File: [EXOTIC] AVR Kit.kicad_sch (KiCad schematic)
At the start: 22 parts, among them J1 AVR-ISP-10, J3 USB_B, J4 Port A, J5 Port B, J6 Port C + D7, J7 Port D, SW1 SW_Push, U1 ATmega32A-P, U6 CH340C, Y1 16 MHz

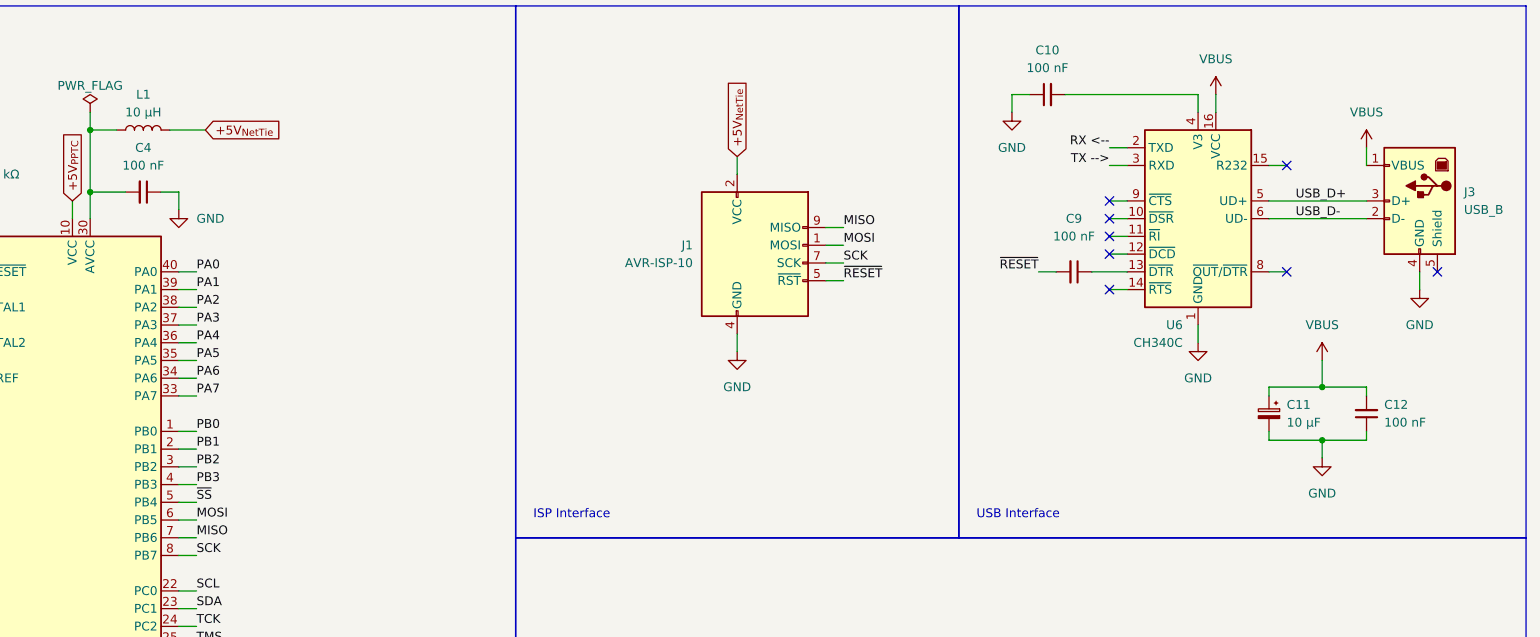
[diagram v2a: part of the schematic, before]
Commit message: Removed the two LED indicators
Removed the two LED indicators for each power source and replaced them with a single LED for the final 5V rail
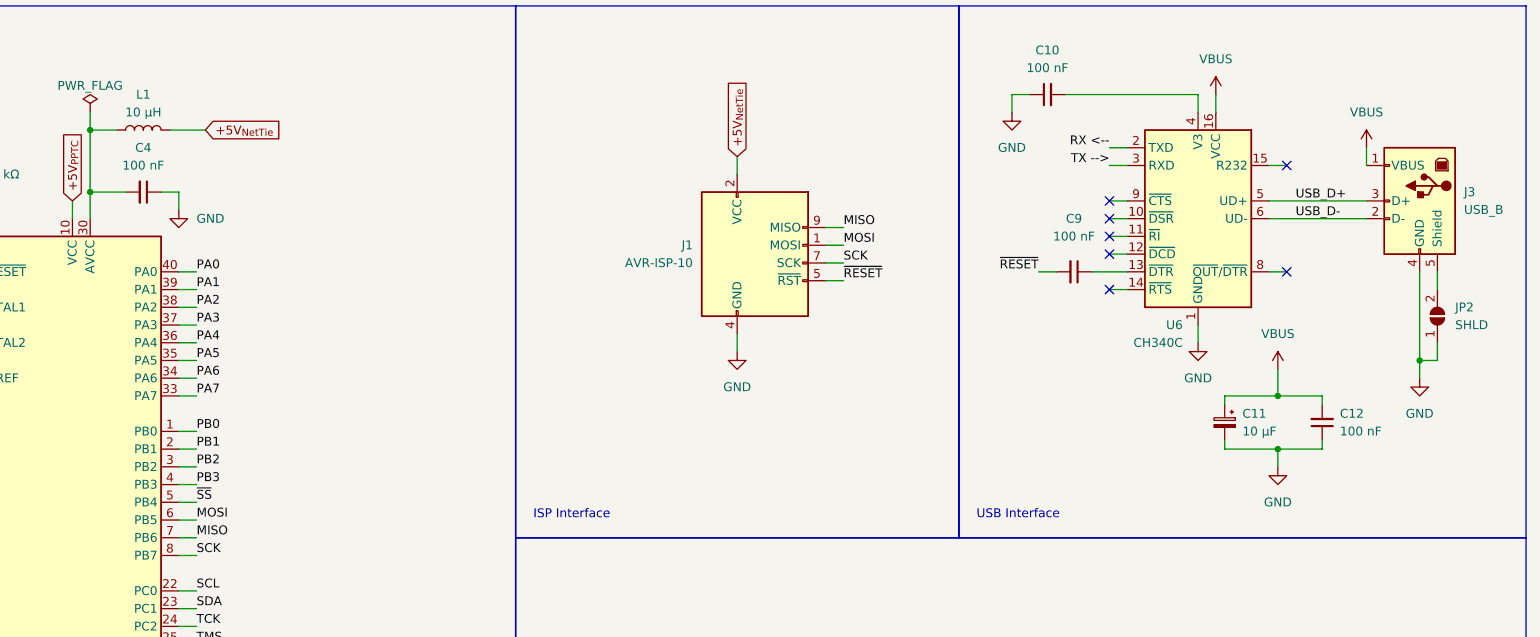
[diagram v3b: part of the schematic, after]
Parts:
- added JP2: SHLD, Jumper:SolderJumper-2_P1.3mm_Open_RoundedPad1.0x1.5mm, symbol Jumper:SolderJumper_2_Open
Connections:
- net +5V_{NetTie}: now also L1.1; no longer L1.2
- net GND: now also JP2.1 (A)
- net at C4.2, U1.30 (AVCC): now also L1.2; no longer L1.1
- net at J3.5 (Shield): now also JP2.2 (B)
- no-connect marks 8 -> 7
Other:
- company: Exotic Racing Team -> Team Exotic
- moved on the sheet: C11, C12, L1
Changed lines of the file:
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@@
 	(title_block
 		(title "ATMEGA32A AVR Kit")
-		(date "2023-10-28")
-		(rev "C1.2")
-		(company "Exotic Racing Team")
+		(date "2024-06-14")
+		(rev "C2.7")
+		(company "Team Exotic")
 		(comment 1 "Author: Morad Tamer")
 	)
@@
 	)
 	(junction
-		(at 255.27 67.31)
+		(at 248.92 68.58)
+		(diameter 0)
+		(color 0 0 0 0)
+	)
+	(junction
+		(at 269.24 63.5)
 		(diameter 0)
 		(color 0 0 0 0)
@@
 	)
 	(junction
-		(at 255.27 74.93)
+		(at 248.92 76.2)
 		(diameter 0)
 		(color 0 0 0 0)
@@
 	)
 	(no_connect
-		(at 271.78 50.8)
-	)
-	(no_connect
 		(at 224.79 45.72)
 	)
@@
 	(wire
 		(pts
-			(xy 247.65 67.31) (xy 247.65 68.58)
+			(xy 241.3 68.58) (xy 241.3 69.85)
 		)
 		(stroke
@@
 	(wire
 		(pts
-			(xy 261.62 73.66) (xy 261.62 74.93)
+			(xy 255.27 74.93) (xy 255.27 76.2)
 		)
 		(stroke
@@
 	(wire
 		(pts
-			(xy 247.65 74.93) (xy 255.27 74.93)
+			(xy 241.3 76.2) (xy 248.92 76.2)
 		)
 		(stroke
@@
 	(wire
 		(pts
+			(xy 271.78 50.8) (xy 271.78 53.34)
+		)
+		(stroke
+			(width 0)
+			(type default)
+		)
+	)
+	(wire
+		(pts
 			(xy 91.44 109.22) (xy 93.98 109.22)
 		)
@@
 	(wire
 		(pts
-			(xy 255.27 63.5) (xy 255.27 67.31)
+			(xy 248.92 64.77) (xy 248.92 68.58)
 		)
 		(stroke
@@
 	(wire
 		(pts
-			(xy 255.27 74.93) (xy 255.27 77.47)
+			(xy 248.92 76.2) (xy 248.92 78.74)
 		)
 		(stroke
@@
 	(wire
 		(pts
-			(xy 255.27 74.93) (xy 261.62 74.93)
+			(xy 248.92 76.2) (xy 255.27 76.2)
 		)
 		(stroke
@@
 	(wire
 		(pts
-			(xy 269.24 50.8) (xy 269.24 53.34)
+			(xy 269.24 50.8) (xy 269.24 63.5)
 		)
 		(stroke
@@
 	(wire
 		(pts
-			(xy 255.27 67.31) (xy 261.62 67.31)
+			(xy 248.92 68.58) (xy 255.27 68.58)
 		)
 		(stroke
@@
 	(wire
 		(pts
+			(xy 271.78 60.96) (xy 271.78 63.5)
+		)
+		(stroke
+			(width 0)
+			(type default)
+		)
+	)
+	(wire
+		(pts
 			(xy 189.23 114.3) (xy 194.31 114.3)
 		)
@@
 	(wire
 		(pts
-			(xy 261.62 67.31) (xy 261.62 68.58)
+			(xy 255.27 68.58) (xy 255.27 69.85)
 		)
 		(stroke
@@
 	(wire
 		(pts
+			(xy 269.24 63.5) (xy 271.78 63.5)
+		)
+		(stroke
+			(width 0)
+			(type default)
+		)
+	)
+	(wire
+		(pts
 			(xy 91.44 76.2) (xy 93.98 76.2)
 		)
@@
 	(wire
 		(pts
+			(xy 269.24 63.5) (xy 269.24 66.04)
+		)
+		(stroke
+			(width 0)
+			(type default)
+		)
+	)
+	(wire
+		(pts
 			(xy 50.8 66.04) (xy 50.8 68.58)
 		)
@@
 	(wire
 		(pts
-			(xy 247.65 67.31) (xy 255.27 67.31)
+			(xy 241.3 68.58) (xy 248.92 68.58)
 		)
 		(stroke
@@
 	(wire
 		(pts
-			(xy 247.65 73.66) (xy 247.65 74.93)
+			(xy 241.3 74.93) (xy 241.3 76.2)
 		)
 		(stroke
@@
 	(symbol
 		(lib_id "power:GND")
-		(at 255.27 77.47 0)
+		(at 248.92 78.74 0)
 		(unit 1)
 		(exclude_from_sim no)
@@
 		(fields_autoplaced yes)
 		(property "Reference" "#PWR023"
-			(at 255.27 83.82 0)
+			(at 248.92 85.09 0)
 			(effects
 				(font
@@
 		)
 		(property "Value" "GND"
-			(at 255.27 82.55 0)
+			(at 248.92 83.82 0)
 			(effects
 				(font
@@
 		)
 		(property "Footprint" ""
-			(at 255.27 77.47 0)
+			(at 248.92 78.74 0)
 			(effects
 				(font
@@
 		)
 		(property "Datasheet" ""
-			(at 255.27 77.47 0)
+			(at 248.92 78.74 0)
 			(effects
 				(font
@@
 		)
 		(property "Description" ""
-			(at 255.27 77.47 0)
+			(at 248.92 78.74 0)
 			(effects
 				(font
@@
 	(symbol
 		(lib_id "power:GND")
-		(at 269.24 53.34 0)
+		(at 269.24 66.04 0)
 		(mirror y)
 		(unit 1)
@@
 		(fields_autoplaced yes)
 		(property "Reference" "#PWR020"
-			(at 269.24 59.69 0)
+			(at 269.24 72.39 0)
 			(effects
 				(font
@@
 		)
 		(property "Value" "GND"
-			(at 269.24 58.42 0)
+			(at 269.24 71.12 0)
 			(effects
 				(font
@@
 		)
 		(property "Footprint" ""
-			(at 269.24 53.34 0)
+			(at 269.24 66.04 0)
 			(effects
 				(font
@@
 		)
 		(property "Datasheet" ""
-			(at 269.24 53.34 0)
+			(at 269.24 66.04 0)
 			(effects
 				(font
@@
 		)
 		(property "Description" ""
-			(at 269.24 53.34 0)
+			(at 269.24 66.04 0)
 			(effects
 				(font
@@
 	(symbol
 		(lib_id "Device:C_Small")
-		(at 261.62 71.12 180)
+		(at 255.27 72.39 180)
 		(unit 1)
 		(exclude_from_sim no)
@@
 		(fields_autoplaced yes)
 		(property "Reference" "C12"
-			(at 264.16 69.8435 0)
+			(at 257.81 71.1135 0)
 			(effects
 				(font
@@
 		)
 		(property "Value" "100 nF"
-			(at 264.16 72.3835 0)
+			(at 257.81 73.6535 0)
 			(effects
 				(font
@@
 		)
 		(property "Footprint" "Capacitor_SMD:C_1206_3216Metric_Pad1.33x1.80mm_HandSolder"
-			(at 261.62 71.12 0)
+			(at 255.27 72.39 0)
 			(effects
 				(font
@@
 		)
 		(property "Datasheet" "~"
-			(at 261.62 71.12 0)
+			(at 255.27 72.39 0)
 			(effects
 				(font
@@
 		)
 		(property "Description" "Unpolarized capacitor, small symbol"
-			(at 261.62 71.12 0)
+			(at 255.27 72.39 0)
 			(effects
 				(font
@@
 		)
 		(property "Local Seller" "https://makerselectronics.com/product/multilayer-ceramic-capacitors-mlcc-smd-smt-50v-100nf-x7r-%c2%b110-1206"
-			(at 261.62 71.12 0)
+			(at 255.27 72.39 0)
 			(effects
 				(font
@@
 	(symbol
 		(lib_id "Device:L")
-		(at 86.36 30.48 90)
+		(at 86.36 30.48 270)
+		(mirror x)
 		(unit 1)
 		(exclude_from_sim no)
@@
 		(on_board yes)
 		(dnp no)
-		(fields_autoplaced yes)
 		(property "Reference" "L1"
 			(at 86.36 25.4 90)
@@
 	(symbol
 		(lib_id "power:VBUS")
-		(at 255.27 63.5 0)
+		(at 248.92 64.77 0)
 		(unit 1)
 		(exclude_from_sim no)
@@
 		(fields_autoplaced yes)
 		(property "Reference" "#PWR017"
-			(at 255.27 67.31 0)
+			(at 248.92 68.58 0)
 			(effects
 				(font
@@
 		)
 		(property "Value" "VBUS"
-			(at 255.27 58.42 0)
+			(at 248.92 59.69 0)
 			(effects
 				(font
@@
 		)
 		(property "Footprint" ""
-			(at 255.27 63.5 0)
+			(at 248.92 64.77 0)
 			(effects
 				(font
@@
 		)
 		(property "Datasheet" ""
-			(at 255.27 63.5 0)
+			(at 248.92 64.77 0)
 			(effects
 				(font
@@
 		)
 		(property "Description" ""
-			(at 255.27 63.5 0)
+			(at 248.92 64.77 0)
 			(effects
 				(font
@@
 	)
 	(symbol
+		(lib_id "Jumper:SolderJumper_2_Open")
+		(at 271.78 57.15 90)
+		(unit 1)
+		(exclude_from_sim no)
+		(in_bom yes)
+		(on_board yes)
+		(dnp no)
+		(fields_autoplaced yes)
+		(property "Reference" "JP2"
+			(at 274.32 55.8799 90)
+			(effects
+				(font
+					(size 1.27 1.27)
+				)
+				(justify right)
+			)
+		)
+		(property "Value" "SHLD"
+			(at 274.32 58.4199 90)
+			(effects
+				(font
+					(size 1.27 1.27)
+				)
+				(justify right)
+			)
+		)
+		(property "Footprint" "Jumper:SolderJumper-2_P1.3mm_Open_RoundedPad1.0x1.5mm"
+			(at 271.78 57.15 0)
+			(effects
+				(font
+					(size 1.27 1.27)
+				)
+				(hide yes)
+			)
+		)
+		(property "Datasheet" "~"
+			(at 271.78 57.15 0)
+			(effects
+				(font
+					(size 1.27 1.27)
+				)
+				(hide yes)
+			)
+		)
+		(property "Description" ""
+			(at 271.78 57.15 0)
+			(effects
+				(font
+					(size 1.27 1.27)
+				)
+				(hide yes)
+			)
+		)
+		(pin "1"
+		)
+		(pin "2"
+		)
+		(instances
+			(project "[EXOTIC] AVR Kit"
+				(path "/bd689b4b-40d7-46ba-91b6-965ce30f8212"
+					(reference "JP2")
+					(unit 1)
+				)
+			)
+		)
+	)
+	(symbol
 		(lib_id "Device:C_Polarized_Small")
-		(at 247.65 71.12 0)
+		(at 241.3 72.39 0)
 		(mirror y)
 		(unit 1)
@@
 		(dnp no)
 		(property "Reference" "C11"
-			(at 250.19 69.85 0)
+			(at 243.84 71.12 0)
 			(effects
 				(font
@@
 		)
 		(property "Value" "10 µF"
-			(at 250.19 72.39 0)
+			(at 243.84 73.66 0)
 			(effects
 				(font
@@
 		)
 		(property "Footprint" "Capacitor_SMD:C_1206_3216Metric_Pad1.33x1.80mm_HandSolder"
-			(at 247.65 71.12 0)
+			(at 241.3 72.39 0)
 			(effects
 				(font
@@
 		)
 		(property "Datasheet" "~"
-			(at 247.65 71.12 0)
+			(at 241.3 72.39 0)
 			(effects
 				(font
@@
 		)
 		(property "Description" "Polarized capacitor, small symbol"
-			(at 247.65 71.12 0)
+			(at 241.3 72.39 0)
 			(effects
 				(font
@@
 		)
 		(property "Local Seller" "https://makerselectronics.com/product/multilayer-ceramic-capacitors-mlcc-smd-smt-10uf-25v-x5r-%c2%b110-1206"
-			(at 247.65 71.12 0)
+			(at 241.3 72.39 0)
 			(effects
 				(font
